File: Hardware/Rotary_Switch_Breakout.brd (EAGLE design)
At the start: 33 x 33 mm, 8 parts, among them SW1 1x10

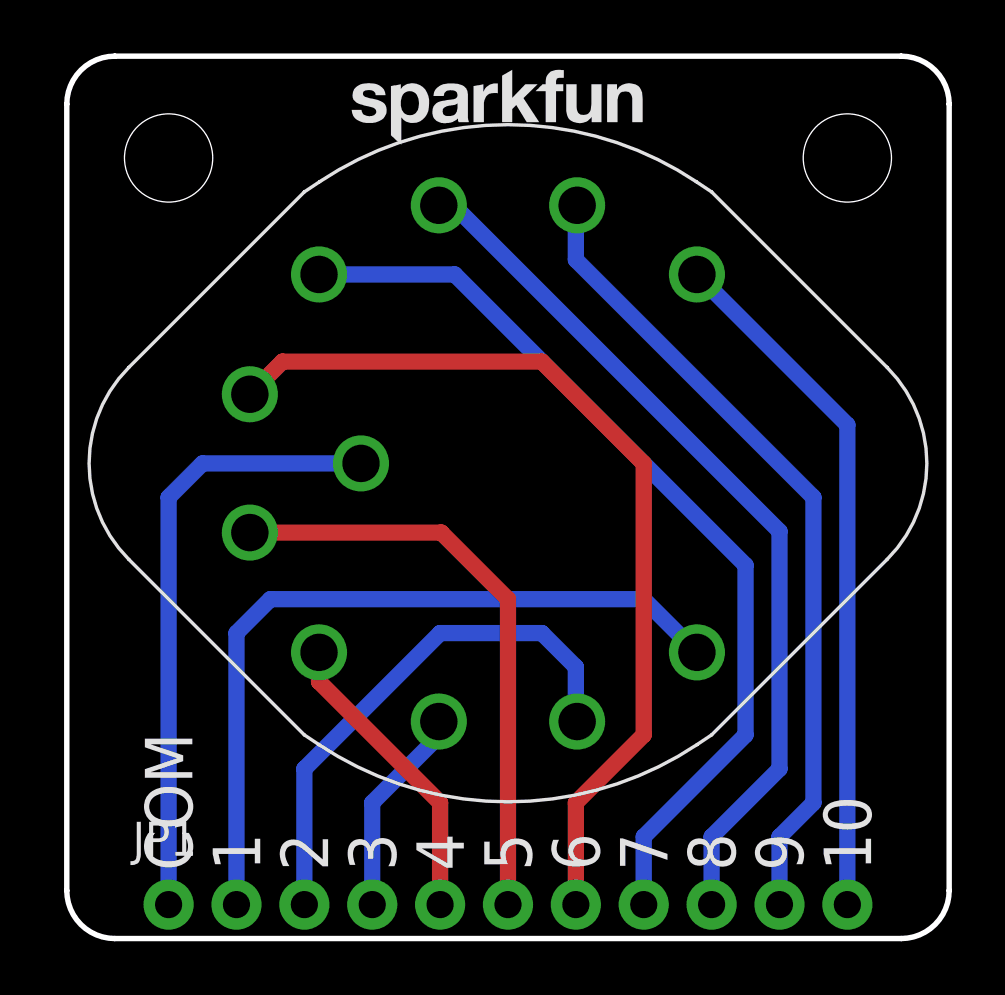
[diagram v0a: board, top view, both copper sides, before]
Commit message: Updates to layout
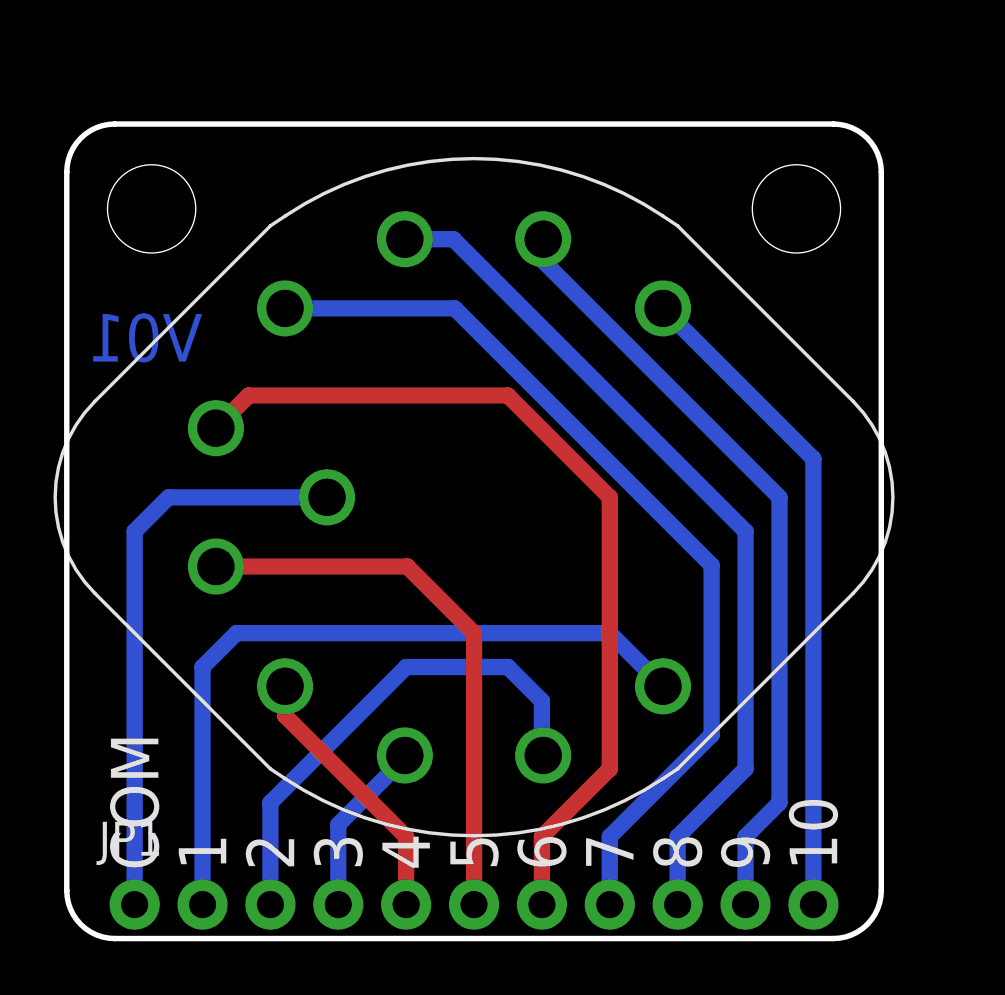
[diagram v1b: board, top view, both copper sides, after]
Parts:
- removed LOGO2: SFE_LOGO_NAME.1_INCH, SparkFun-Aesthetics:SFE_LOGO_NAME_.1
- moved LOGO3 20.3 mm to (21.3, 7.62)
- moved STANDOFF2 2.69 mm to (27.3, 27.3)
- moved STANDOFF1 2.01 mm to (3.17, 27.3)
- moved LOGO1 1.80 mm to (15.2, 14.0)
- moved SW1 1.80 mm to (15.2, 16.5)
- moved JP1 1.27 mm to (2.54, 1.27)
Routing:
- net N$4: track 7.92 -> 6.58 mm
- net N$9: track 33.6 -> 32.3 mm
- net N$7: track 34.4 -> 33.1 mm
- net N$6: track 22.1 -> 20.9 mm
- net N$5: track 11.3 -> 10.0 mm
- net N$3: track 19.9 -> 18.7 mm
- net N$10: track 30.4 -> 29.1 mm
- net N$1: track 23.0 -> 21.7 mm
- net N$2: track 28.7 -> 27.5 mm
- net N$11: track 25.9 -> 24.6 mm
- net N$8: track 34.7 -> 34.2 mm
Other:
- board size 33 x 33 mm -> 30.5 x 30.5 mm
- board text added: "V01"
